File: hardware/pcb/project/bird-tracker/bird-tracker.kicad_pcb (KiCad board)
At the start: 2 copper layers, 11 parts, among them U1 STM32U031R8T6, U2 SAM-M10Q-00B, U3 SIM7080G, U4 LSM6DS3TR, U5 STTS22HTR, X1 ABS07-32.768KHZ-7-T

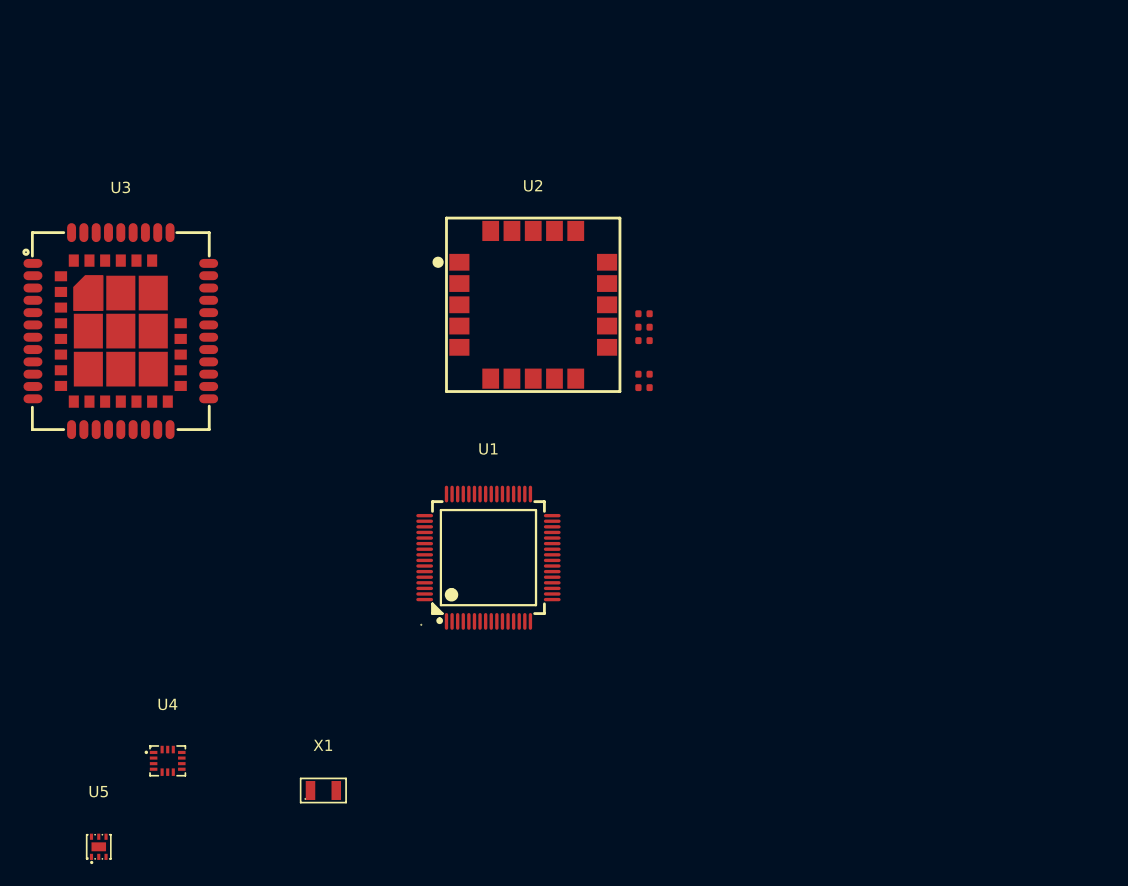
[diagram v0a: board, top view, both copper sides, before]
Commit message: Sensors sheet complete
Revision v0.1
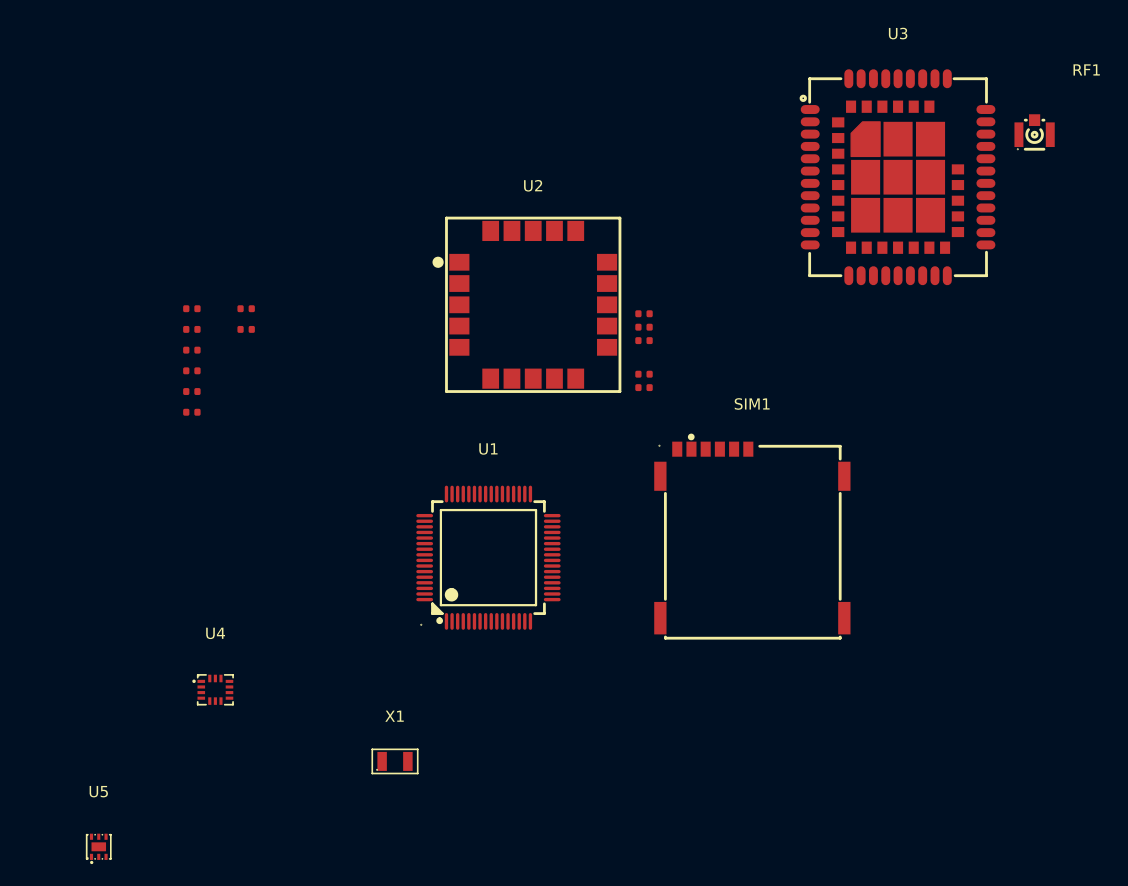
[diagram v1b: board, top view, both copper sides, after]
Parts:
- added C2: 100nF, PCM_JLCPCB:C_0402, F.Cu at (99.7, 54.1)
- added C3: 100nF, PCM_JLCPCB:C_0402, F.Cu at (99.7, 56.0)
- added C4: 10uF, PCM_JLCPCB:C_0402, F.Cu at (99.7, 57.9)
- added C5: 100nF, PCM_JLCPCB:C_0402, F.Cu at (99.7, 59.7)
- added R2: 2.2kΩ, PCM_JLCPCB:R_0402, F.Cu at (104.5, 54.1)
- added R3: 2.2kΩ, PCM_JLCPCB:R_0402, F.Cu at (104.5, 56.0)
- added R5: 10kΩ, PCM_JLCPCB:R_0402, F.Cu at (99.7, 61.5)
- added R6: 10kΩ, PCM_JLCPCB:R_0402, F.Cu at (99.7, 63.4)
- added RF1: U.FL-R-SMT, bird-tracker:ANT-SMD_U.FL-R-SMT10, F.Cu at (175.0, 38.0)
- added SIM1: MICRO SIM 6P H1.35, bird-tracker:SIM-SMD_MICRO-SIM-6P-H1.35, F.Cu at (149.8, 74.2)
- moved U3 70.8 mm to (162.8, 42.4)
- moved U4 7.65 mm to (101.8, 88.2)
- moved X1 6.91 mm to (117.8, 94.6)
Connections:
- net GPS_INT renamed GNSS_INT
- net GPS_RST renamed GNSS_RST
- R1 pad 2: GPS_SCL -> GNSS_SCL
- R4 pad 1: GPS_SDA -> GNSS_SDA
- U2 pad 3: +3.3V -> GNSS_BCKP
- U3 pad 13: unconnected-(U3-GND-Pad13) -> GND
- U3 pad 19: unconnected-(U3-GND-Pad19) -> GND
- U3 pad 21: unconnected-(U3-GND-Pad21) -> GND
- U3 pad 27: unconnected-(U3-GND-Pad27) -> GND
- U3 pad 30: unconnected-(U3-GND-Pad30) -> GND
- U3 pad 31: unconnected-(U3-GND-Pad31) -> GND
- U3 pad 32: unconnected-(U3-RF_ANT-Pad32) -> Net-(RF1-SIG)
- U3 pad 33: unconnected-(U3-GND-Pad33) -> GND
- U3 pad 36: unconnected-(U3-GND-Pad36) -> GND
- U3 pad 37: unconnected-(U3-GND-Pad37) -> GND
- U3 pad 45: unconnected-(U3-GND-Pad45) -> GND
- U3 pad 63: unconnected-(U3-GND-Pad63) -> GND
- U3 pad 66: unconnected-(U3-GND-Pad66) -> GND
- U3 pad 67: unconnected-(U3-GND-Pad67) -> GND
- U3 pad 69: unconnected-(U3-GND-Pad69) -> GND
- U3 pad 70: unconnected-(U3-GND-Pad70) -> GND
- U3 pad 71: unconnected-(U3-GND-Pad71) -> GND
- U3 pad 72: unconnected-(U3-GND-Pad72) -> GND
- U3 pad 73: unconnected-(U3-GND-Pad73) -> GND
- U3 pad 74: unconnected-(U3-GND-Pad74) -> GND
- U3 pad 75: unconnected-(U3-GND-Pad75) -> GND
- U3 pad 76: unconnected-(U3-GND-Pad76) -> GND
- U3 pad 77: unconnected-(U3-GND-Pad77) -> GND
- U3 pad 8: unconnected-(U3-GND-Pad8) -> GND
- U4 pad 1: unconnected-(U4-SDO/SA0-Pad1) -> GND
- U4 pad 12: unconnected-(U4-CS-Pad12) -> +3.3V
- U4 pad 13: unconnected-(U4-SCL-Pad13) -> SENS_SCL
- U4 pad 14: unconnected-(U4-SDA-Pad14) -> SENS_SDA
- U4 pad 2: unconnected-(U4-SDX-Pad2) -> GND
- U4 pad 3: unconnected-(U4-SCX-Pad3) -> GND
- U4 pad 4: unconnected-(U4-INT1-Pad4) -> LSM_INT1
- U4 pad 5: unconnected-(U4-VDDIO-Pad5) -> +3.3V
- U4 pad 6: unconnected-(U4-GND-Pad6) -> GND
- U4 pad 7: unconnected-(U4-GND-Pad7) -> GND
- U4 pad 8: unconnected-(U4-VDD-Pad8) -> +3.3V
- U4 pad 9: unconnected-(U4-INT2-Pad9) -> LSM_INT2
- U5 pad 1: unconnected-(U5-SCL-Pad1) -> SENS_SCL
- U5 pad 2: unconnected-(U5-ALERT/INT-Pad2) -> STT_INT
- U5 pad 3: unconnected-(U5-VDD-Pad3) -> +3.3V
- U5 pad 4: unconnected-(U5-Addr-Pad4) -> GND
- U5 pad 5: unconnected-(U5-GND-Pad5) -> GND
- U5 pad 6: unconnected-(U5-SDA-Pad6) -> SENS_SDA
- U5 pad 7: unconnected-(U5-EP-Pad7) -> GND
